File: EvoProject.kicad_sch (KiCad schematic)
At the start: 0 parts

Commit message: Class A Amplifier Schematic Mockup
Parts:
- added C1, C2: 22μF, symbol Device:C_Polarized
- added C3: 220μF, symbol Device:C_Polarized
- added LS1: Speaker, symbol Device:Speaker
- added Q1, Q2: 2N3904, Package_TO_SOT_THT:TO-92_Inline, symbol Transistor_BJT:2N3904
- added R1: 4.7k, symbol Device:R_US
- added R2: 820k, symbol Device:R_US
- added R3: 6.8k, symbol Device:R_US
- added R4: 10k, symbol Device:R_US
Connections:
- new net: C2.1, Q1.3 (C), R1.2
- new net: C2.2, Q2.2 (B), R3.2, R4.1
- new net: C1.1, Q1.2 (B), R2.1
- new net: C3.1, Q2.1 (E)
- new net: C3.2, LS1.1
- new net +9V: Q2.3 (C), R1.1, R2.2, R3.1
- new net AC: C1.2
- new net GND: LS1.2, Q1.1 (E), R4.2

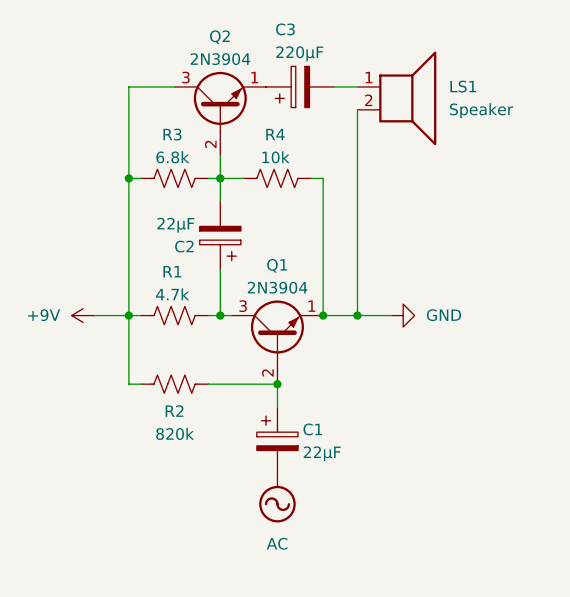
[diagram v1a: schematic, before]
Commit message: Voltage Divider Class A Amp
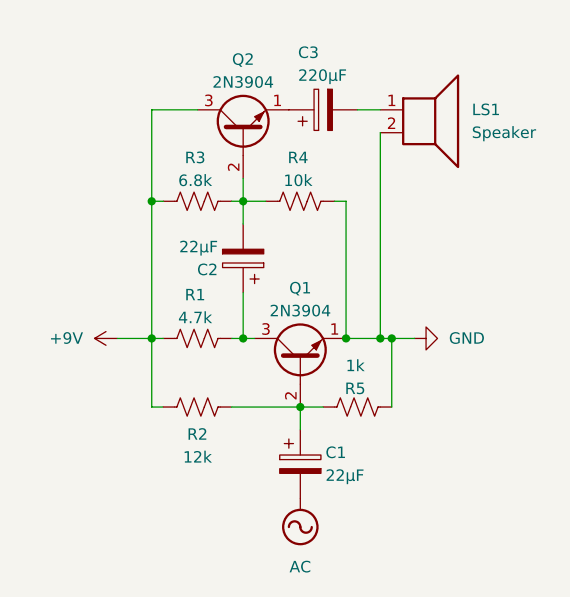
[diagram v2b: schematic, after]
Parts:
- added R5: 1k, symbol Device:R_US
- R2: value 820k -> 12k
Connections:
- net GND: now also R5.2
- net at C1.1, Q1.2 (B), R2.1: now also R5.1
